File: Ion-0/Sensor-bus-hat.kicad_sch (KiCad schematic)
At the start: 89 parts, among them J10 Conn_Heater, J11 Conn_01x02, J12 Conn_01x02, J13 Conn_01x04, J6 Coaxial_Small, J7 Conn_01x02, J8 Conn_Heater, J9 Conn_Heater, Q1 IRLML6244, Q2 IRLML6244, Q3 IRLML6244, Q4 IRLML6244, U2 LMT84DCK, U3 BNO085, U4 TCA9617ADGKR, U5 LMT84DCK, U6 MAX-M10M-00B, U7 TPS3850H50DRCR, U8 SN65HVD230, U9 MS860702BA01-50, Y2 9HT10-32.768KBZF-T

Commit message: restarting layout
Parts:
- removed C22: 1uF, Capacitor_SMD:C_0603_1608Metric, symbol Device:C_Small
- removed J10: Conn_Heater, Connector_JST:JST_SH_SM02B-SRSS-TB_1x02-1MP_P1.00mm_Horizontal, symbol Connector_Generic:Conn_01x02
- removed J7: Conn_01x02, Connector_JST:JST_SH_SM02B-SRSS-TB_1x02-1MP_P1.00mm_Horizontal, symbol Connector_Generic:Conn_01x02
- removed JP1, JP2, JP3, JP4: SolderJumper_2_Open, Jumper:SolderJumper-2_P1.3mm_Open_TrianglePad1.0x1.5mm, symbol Jumper:SolderJumper_2_Open
- removed Q3, Q4: IRLML6244, Package_TO_SOT_SMD:SOT-23, symbol Transistor_FET:IRLML6244
- removed U2, U5: LMT84DCK, Package_TO_SOT_SMD:SOT-353_SC-70-5, symbol Sensor_Temperature:LMT84DCK
- removed U9: MS860702BA01-50, 1_Ion:MS860702BA01-50_TEC, symbol 1_ion_library:MS860702BA01-50
- added D10: TVS_3V3, Diode_SMD:D_0402_1005Metric_Pad0.77x0.64mm_HandSolder, symbol Diode:SM6T33A
- added J10: Conn_CAN, Connector_JST:JST_SH_BM04B-SRSS-TB_1x04-1MP_P1.00mm_Vertical, symbol Connector_Generic:Conn_01x04
- added R39, R40: 0, Resistor_SMD:R_1206_3216Metric, symbol Device:R_Small_US
- added R41: 100K, Resistor_SMD:R_0603_1608Metric_Pad0.98x0.95mm_HandSolder, symbol Device:R_Small_US
- added R42, R47: 0, symbol Device:R_Small_US
- added R43, R44, R45, R46: 0, Resistor_SMD:R_0603_1608Metric_Pad0.98x0.95mm_HandSolder, symbol Device:R_Small_US
- added TH3: 100K@25C, symbol Device:Thermistor_NTC
- added U1: HDC2080, Sensor_Humidity:Texas_S-PWSON-N6-HDC2080, symbol Sensor_Humidity:HDC2080
- added U2: MS5607-02BA, Package_LGA:LGA-8_3x5mm_P1.25mm, symbol Sensor_Pressure:MS5607-02BA
- C1: value 220nF -> 100nF
- C7: value 1uF -> 100nF
- J11: value Conn_01x02 -> Conn_Prob_1; footprint Connector_JST:JST_SH_SM02B-SRSS-TB_1x02-1MP_P1.00mm_Horizontal -> TerminalBlock:TerminalBlock_Xinya_XY308-2.54-2P_1x02_P2.54mm_Horizontal
- J12: value Conn_01x02 -> Conn_Prob_2; footprint Connector_JST:JST_SH_SM02B-SRSS-TB_1x02-1MP_P1.00mm_Horizontal -> TerminalBlock:TerminalBlock_Xinya_XY308-2.54-2P_1x02_P2.54mm_Horizontal
- J6: footprint Connector_Coaxial:SMA_Samtec_SMA-J-P-H-ST-EM1_EdgeMount -> Connector_Coaxial:U.FL_Molex_MCRF_73412-0110_Vertical
- J8: footprint Connector_JST:JST_SH_SM02B-SRSS-TB_1x02-1MP_P1.00mm_Horizontal -> TerminalBlock:TerminalBlock_Xinya_XY308-2.54-2P_1x02_P2.54mm_Horizontal
- J9: value Conn_Heater -> Conn_prob_3; footprint Connector_JST:JST_SH_SM02B-SRSS-TB_1x02-1MP_P1.00mm_Horizontal -> TerminalBlock:TerminalBlock_Xinya_XY308-2.54-2P_1x02_P2.54mm_Horizontal
- R29: value 330 -> 100
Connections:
- net +1V8: now also R41.1; no longer C7.1
- net +3V3: now also C7.1, D10.1 (A1), J10.4 (Pin_4), R47.1, U1.5 (VDD), U2.1 (VDD), U2.2 (PS)
- net +5V: now also R39.1; no longer J8.1 (Pin_1), J9.1 (Pin_1)
- net AIN1: now also J12.1 (Pin_1), R4.2
- net AIN2: now also J9.1 (Pin_1), R41.2; no longer J12.1 (Pin_1), R4.2
- net CAN_N: now also J10.2 (Pin_2)
- net CAN_P: now also J10.1 (Pin_1)
- net GND: now also J9.2 (Pin_2), Q1.2 (S), Q2.2 (S), D10.2 (A2), J10.3 (Pin_3), R42.2, U1.2 (GND), U2.3 (GND); no longer Q1.3 (D), Q2.3 (D)
- net GPS-RX: now also R46.2
- net GPS-TX: now also R45.1
- net I2C1_SCL: now also R44.1, U1.6 (SCL), U2.8 (SCLK)
- net I2C1_SDA: now also R43.1, U1.1 (SDA), U2.7 (SDI/SDA)
- net at U6.3 (RXD): now also R46.1
- net at BZ1.2 (-), R21.2: now also Q1.3 (D); no longer Q1.2 (S)
- net at U6.16 (SDA): now also R43.2
- net at U6.17 (SCL): now also R44.2
- net at U6.2 (TXD): now also R45.2
- net at J8.2 (Pin_2): now also R39.2, R40.2; no longer Q2.2 (S)
- new net: R42.1, U2.4 (CSB), U2.5 (CSB)
- new net: R47.2, U1.3 (ADDR)
- new net: J8.1 (Pin_1), Q2.3 (D)
- new net +12V: R40.1
- new net Humidity-INT: U1.4 (DRDY)
- no-connect marks 16 -> 19
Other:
- note added: "Barometer"
- note added: "Humidity Sensor"
- note removed: "Barometer + Temp + Humidity"
- note removed: "Temperature Sensors"
- moved on the sheet: J11, J12, J8, Q2, R1, R11, R2, R29, R3, R4, R5, TH1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

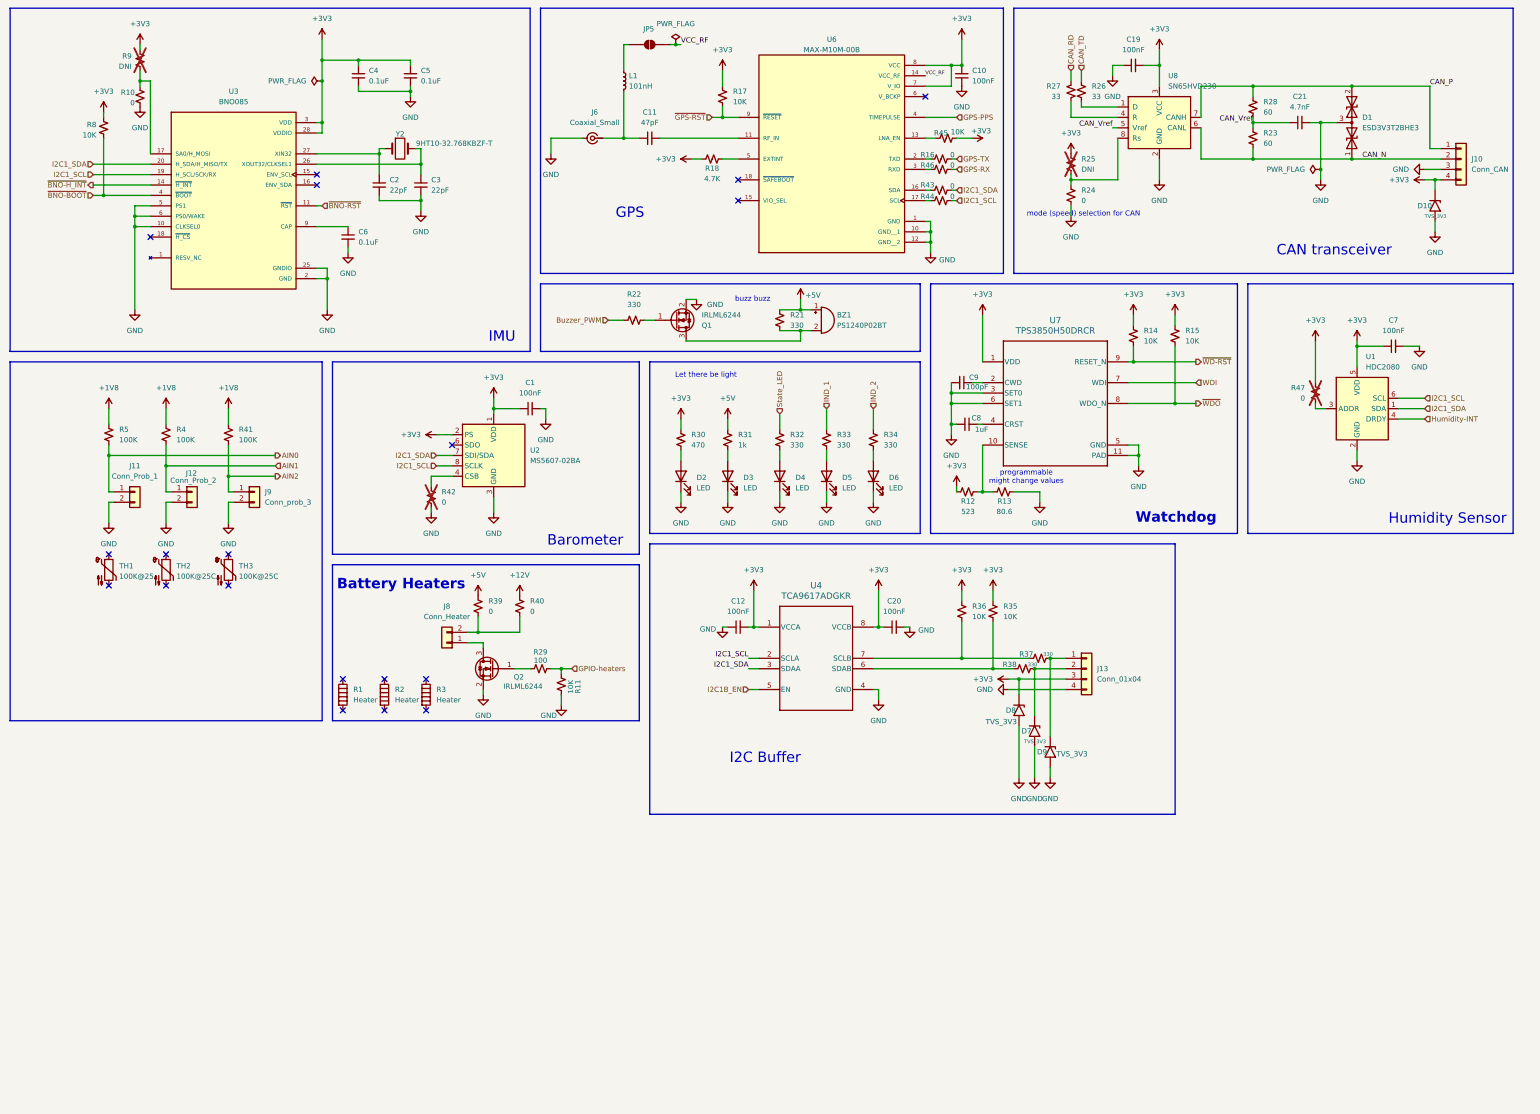
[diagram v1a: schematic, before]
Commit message: the board is done but still needs to be cleaned of schematic up and via stitching
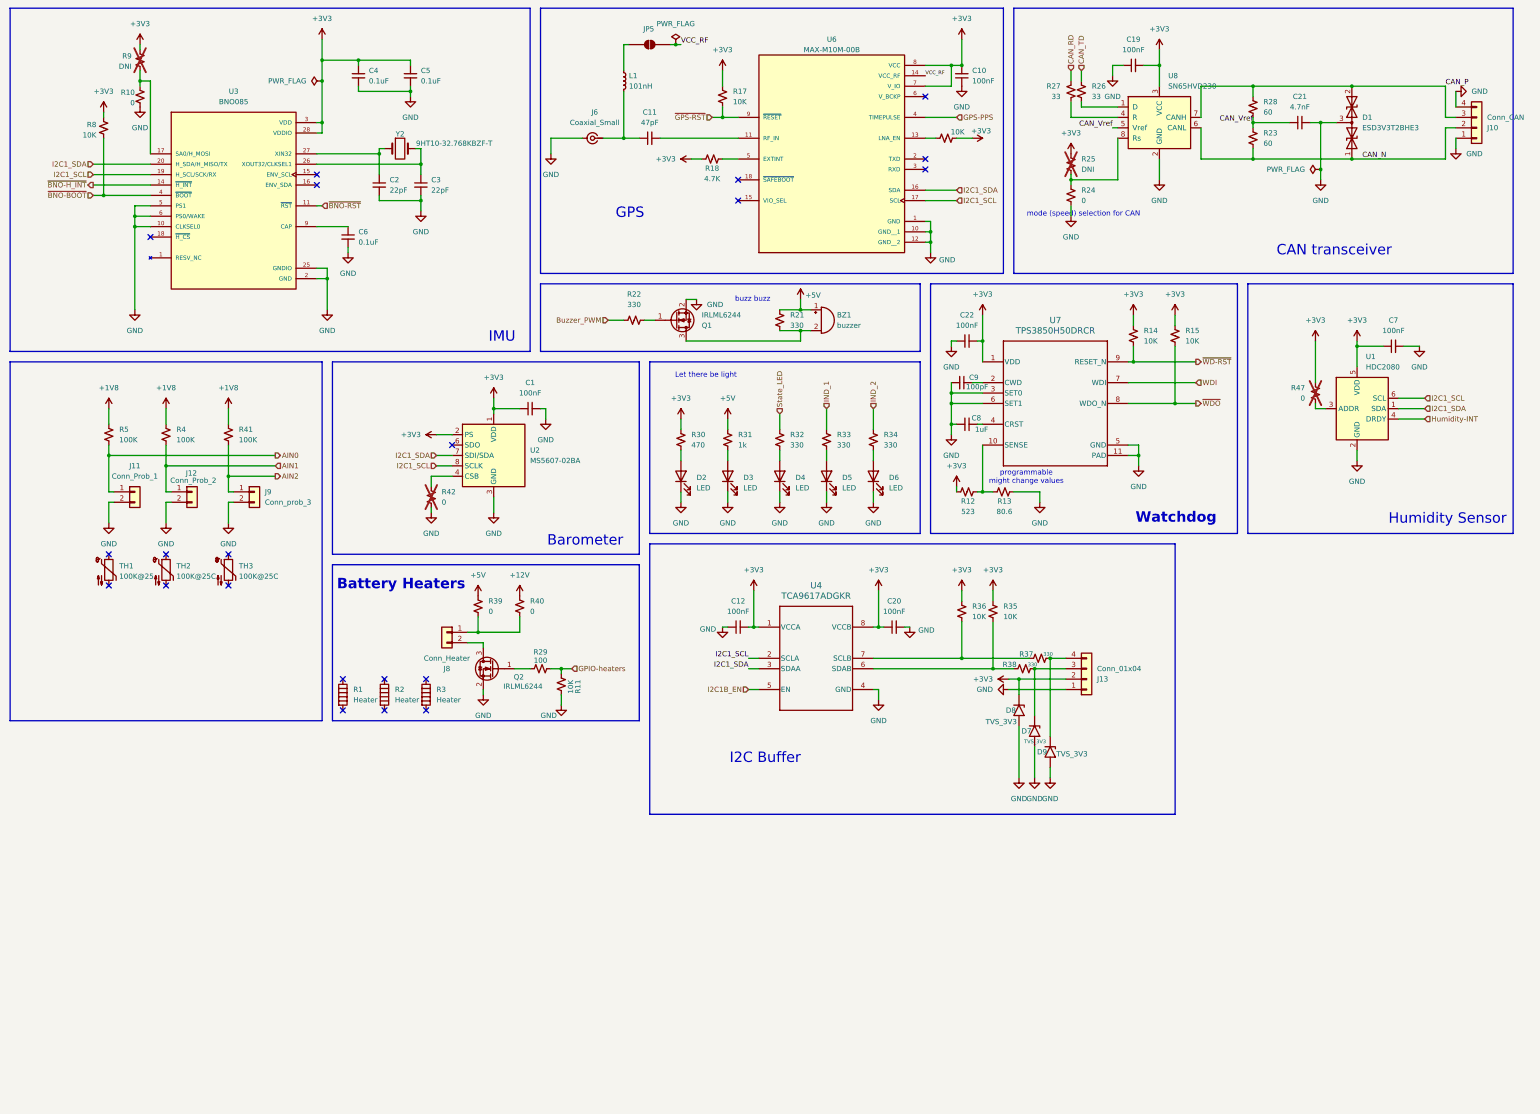
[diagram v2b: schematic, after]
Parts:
- removed D10: TVS_3V3, Diode_SMD:D_0402_1005Metric_Pad0.77x0.64mm_HandSolder, symbol Diode:SM6T33A
- removed R43, R44, R45, R46: 0, Resistor_SMD:R_0603_1608Metric_Pad0.98x0.95mm_HandSolder, symbol Device:R_Small_US
- added C22: 100nF, Capacitor_SMD:C_0603_1608Metric, symbol Device:C_Small
- BZ1: value PS1240P02BT -> buzzer; footprint Buzzer_Beeper:Buzzer_TDK_PS1240P02BT_D12.2mm_H6.5mm -> Buzzer_Beeper:Buzzer_CUI_CPT-9019S-SMT
- D2, D3, D4, D5, D6: footprint LED_SMD:LED_0805_2012Metric -> LED_SMD:LED_0603_1608Metric_Pad1.05x0.95mm_HandSolder
- J10: footprint Connector_JST:JST_SH_BM04B-SRSS-TB_1x04-1MP_P1.00mm_Vertical -> Connector_JST:JST_SH_SM04B-SRSS-TB_1x04-1MP_P1.00mm_Horizontal
- R42, R47: footprint (none) -> Resistor_SMD:R_0603_1608Metric_Pad0.98x0.95mm_HandSolder
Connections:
- net +3V3: now also J13.2 (Pin_2), C22.2; no longer J10.4 (Pin_4), J13.3 (Pin_3)
- net CAN_P: now also J10.3 (Pin_3); no longer J10.1 (Pin_1)
- net GND: now also J10.1 (Pin_1), J10.4 (Pin_4), J13.1 (Pin_1), C22.1; no longer J10.3 (Pin_3), J13.4 (Pin_4)
- net I2C1_SCL: now also U6.17 (SCL)
- net I2C1_SDA: now also U6.16 (SDA)
- net at R39.2, R40.2: now also J8.1 (Pin_1); no longer J8.2 (Pin_2)
- net at D7.1 (A1), R38.2: now also J13.3 (Pin_3); no longer J13.2 (Pin_2)
- net at Q2.3 (D): now also J8.2 (Pin_2); no longer J8.1 (Pin_1)
- net at D9.1 (A1), R37.2: now also J13.4 (Pin_4); no longer J13.1 (Pin_1)
- no-connect marks 19 -> 21
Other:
- moved on the sheet: J10, J8

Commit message: nothing working commit
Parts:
- D7, D8, D9: footprint Diode_SMD:D_0402_1005Metric_Pad0.77x0.64mm_HandSolder -> Diode_SMD:D_0603_1608Metric
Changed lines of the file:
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@@
 			)
 		)
-		(property "Footprint" "Diode_SMD:D_0402_1005Metric_Pad0.77x0.64mm_HandSolder"
+		(property "Footprint" "Diode_SMD:D_0603_1608Metric"
 			(at 256.54 185.42 0)
 			(hide yes)
@@
 			)
 		)
-		(property "Footprint" "Diode_SMD:D_0402_1005Metric_Pad0.77x0.64mm_HandSolder"
+		(property "Footprint" "Diode_SMD:D_0603_1608Metric"
 			(at 260.35 190.5 0)
 			(hide yes)
@@
 			)
 		)
-		(property "Footprint" "Diode_SMD:D_0402_1005Metric_Pad0.77x0.64mm_HandSolder"
+		(property "Footprint" "Diode_SMD:D_0603_1608Metric"
 			(at 264.16 195.58 0)
 			(hide yes)

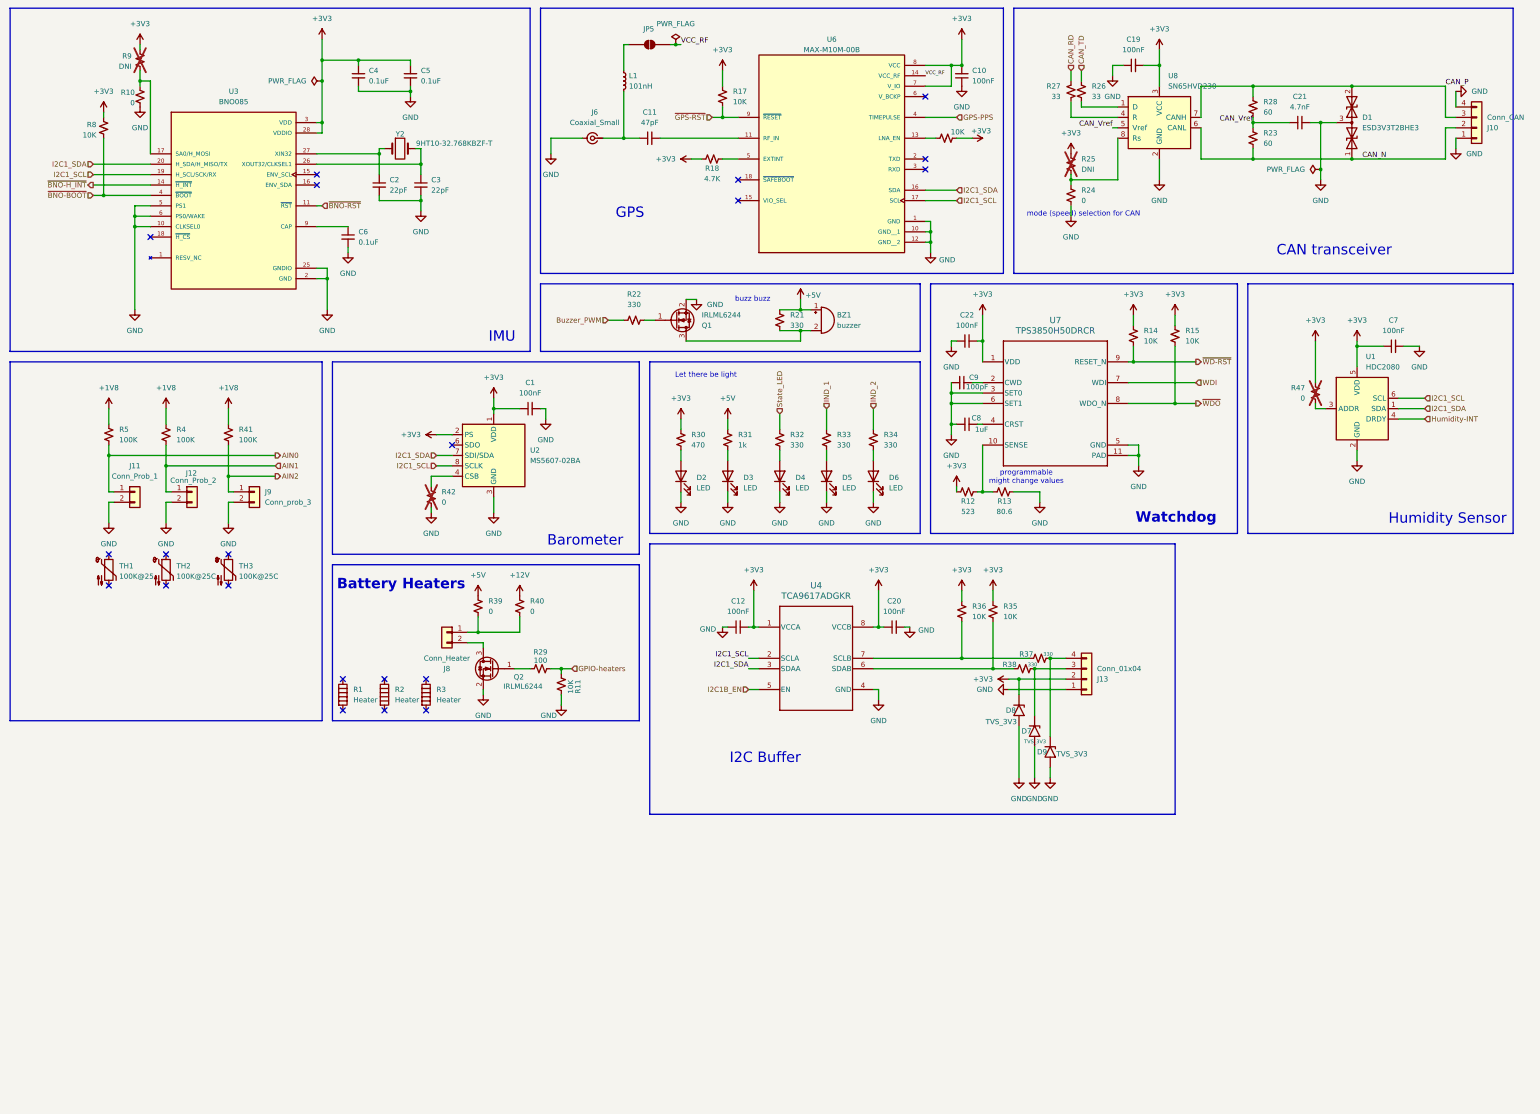
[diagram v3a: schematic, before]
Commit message: added stepper driver
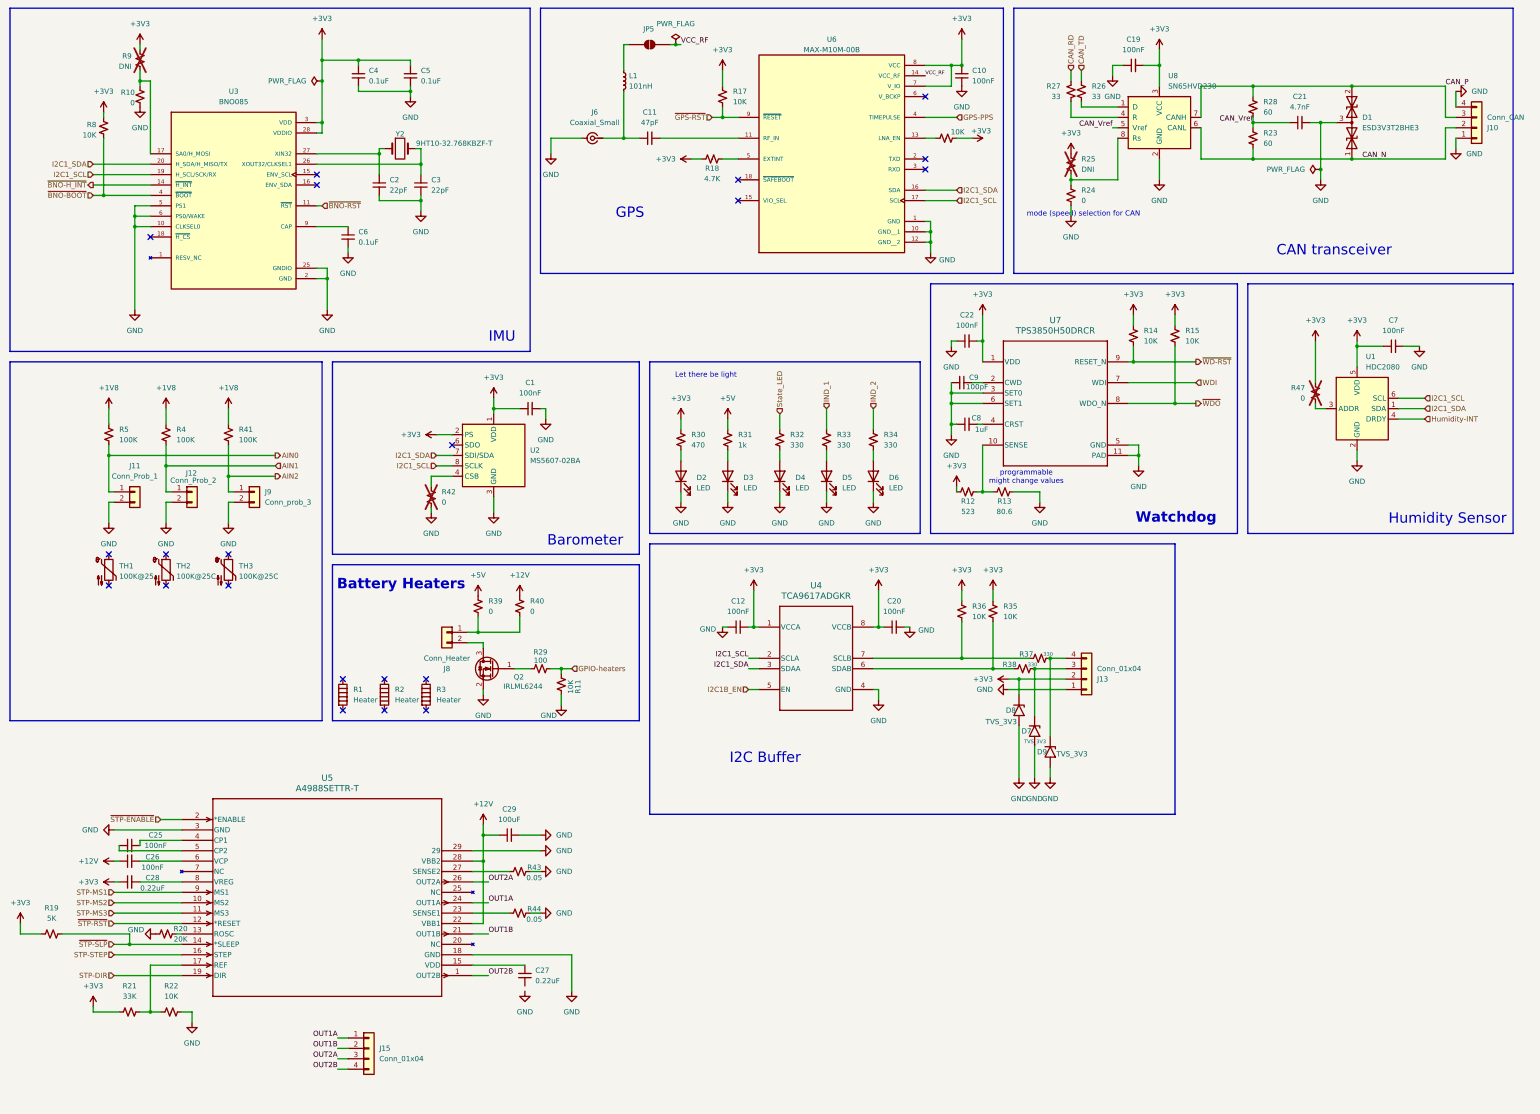
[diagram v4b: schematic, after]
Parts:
- removed BZ1: buzzer, Buzzer_Beeper:Buzzer_CUI_CPT-9019S-SMT, symbol Device:Buzzer
- removed Q1: IRLML6244, Package_TO_SOT_SMD:SOT-23, symbol Transistor_FET:IRLML6244
- added C25, C26: 100nF, symbol Device:C_Small
- added C27, C28: 0.22uF, symbol Device:C_Small
- added C29: 100uF, symbol Device:C_Small
- added J15: Conn_01x04, symbol Connector_Generic:Conn_01x04
- added R19: 5K, symbol Device:R_Small_US
- added R20: 20K, symbol Device:R_Small_US
- added R43, R44: 0.05, symbol Device:R_Small_US
- added U5: A4988SETTR-T, QFN-28_ALM, symbol 1_ion_library:A4988SETTR-T
- R21: value 330 -> 33K; footprint Resistor_SMD:R_0603_1608Metric_Pad0.98x0.95mm_HandSolder -> (none)
- R22: value 330 -> 10K; footprint Resistor_SMD:R_0603_1608Metric_Pad0.98x0.95mm_HandSolder -> (none)
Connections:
- net Buzzer_PWM is gone; now on an unnamed net: R22.1
- net +12V: now also C26.1, C29.1, U5.22 (VBB1), U5.28 (VBB2)
- net +3V3: now also R21.1, C28.1, R19.2
- net +5V: no longer R21.1
- net GND: now also R22.2, C29.2, R20.1, R43.2, R44.2, U5.18 (GND), U5.29, U5.3 (GND)
- net at R21.2: now also U5.17 (REF)
- new net: R20.2, U5.13 (ROSC)
- new net: C26.2, U5.6 (VCP)
- new net: C25.1, U5.4 (CP1)
- new net: C25.2, U5.5 (CP2)
- new net: R44.1, U5.23 (SENSE1)
- new net: C27.1, U5.15 (VDD)
- new net: R43.1, U5.27 (SENSE2)
- new net: C28.2, U5.8 (VREG)
- new net OUT1A: J15.1 (Pin_1), U5.24 (OUT1A)
- new net OUT1B: J15.2 (Pin_2), U5.21 (OUT1B)
- new net OUT2A: J15.3 (Pin_3), U5.26 (OUT2A)
- new net OUT2B: J15.4 (Pin_4), U5.1 (OUT2B)
- new net STP-DIR: U5.19 (DIR)
- new net STP-MS1: U5.9 (MS1)
- new net STP-MS2: U5.10 (MS2)
- new net STP-MS3: U5.11 (MS3)
- new net STP-STEP: U5.16 (STEP)
- new net ~{STP-ENABLE}: U5.2 (*ENABLE)
- new net ~{STP-RST}: U5.12 (*RESET)
- new net ~{STP-SLP}: R19.1, U5.14 (*SLEEP)
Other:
- note removed: "buzz buzz"

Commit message: fixes in the schematic, made it better
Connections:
- net GND: now also C27.2
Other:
- moved on the sheet: C10, C11, C12, C19, C20, C21, C22, C7, C8, C9, D1, D2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
